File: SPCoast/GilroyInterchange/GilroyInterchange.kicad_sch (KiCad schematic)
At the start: 30 parts, among them SW777 777, SW781 781

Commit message: fix(kicad): approach circuits end in T; desk tokens follow
Plants: Christopher 1NA/2NA/1SA/2SA, GilroyCalTrain 1NA/1SA, GilroyInterchange
1SA, Sargent 1NA/1SA/2SA gain the final T (ADR 0003 D4). Sargent's reference
Corporal:2NA becomes Corporal:2NAT, the circuit Corporal draws.

Desk (South-cTc sheets): IndicationToken follows the plants for Christopher,
GilroyCalTrain, GilroyInterchange; Corporal 1SA becomes 1SAT (the plant already
had it); Christopher 815T2 becomes 815AT1 (the OS circuit of switch 815A).

Not changed, awaiting decisions in the dry-run report: 0<n>T renames (IND,
TK<n>, Interchange, 2NAAT, 2SAT), section 2 of an approach, unnamed circuits,
Watsonville, CP_Watsonville: references, 1TK.

Verified: netlists rebuilt for all affected projects; of 33 desk circuit tokens,
5 now match no plant circuit (was 11): 1TK, CP_Watsonville:SA1,
CP_Watsonville:837T1, Watsonville 1NAK and 2NAK. KiCad closed, no ~*.lck.

Co-Authored-By: Claude Sonnet 5.5 <noreply@anthropic.com>
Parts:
- TC1: value 1SA -> 1SAT
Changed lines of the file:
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@@
 			)
 		)
-		(property "Value" "1SA"
+		(property "Value" "1SAT"
 			(at 61.47 74.68 0)
 			(show_name no)

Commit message: SPCoast: owner's edit: GilroyInterchange 1NAT circuit marker (baseline)
Co-Authored-By: Claude Sonnet 5.5 <noreply@anthropic.com>
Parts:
- added TC4: 1NAT, symbol Railroad:Track Circuit
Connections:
- net at B8.2 (B), CP2.1 (To), DOT1.1: now also TC4.1 (MC)
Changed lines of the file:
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@@
 	)
 	(junction
-		(at 184.15 77.47)
+		(at 196.85 77.47)
 		(diameter 0)
 		(color 0 0 0 0)
@@
 	)
 	(junction
+		(at 182.88 77.47)
+		(diameter 0)
+		(color 0 0 0 0)
+	)
+	(junction
 		(at 120.65 77.47)
 		(diameter 0)
@@
 	(wire
 		(pts
+			(xy 182.88 77.47) (xy 196.85 77.47)
+		)
+		(stroke
+			(width 0.4064)
+			(type default)
+		)
+	)
+	(wire
+		(pts
 			(xy 53.34 77.47) (xy 63.5 77.47)
 		)
@@
 	(wire
 		(pts
-			(xy 170.18 77.47) (xy 184.15 77.47)
+			(xy 170.18 77.47) (xy 182.88 77.47)
 		)
 		(stroke
@@
 	(symbol
 		(lib_id "Railroad:NextCP")
-		(at 184.15 77.47 0)
+		(at 196.85 77.47 0)
 		(unit 1)
 		(body_style 1)
@@
 		(dnp no)
 		(property "Reference" "CP2"
-			(at 187.325 79.375 0)
+			(at 200.025 79.375 0)
 			(hide yes)
 			(show_name no)
@@
 		)
 		(property "Value" "Luchessa"
-			(at 195.834 77.216 0)
+			(at 208.534 77.216 0)
 			(show_name no)
 			(do_not_autoplace no)
@@
 		)
 		(property "Footprint" ""
-			(at 180.34 77.47 0)
+			(at 193.04 77.47 0)
 			(hide yes)
 			(show_name no)
@@
 		)
 		(property "Datasheet" ""
-			(at 180.34 77.47 0)
+			(at 193.04 77.47 0)
 			(hide yes)
 			(show_name no)
@@
 		)
 		(property "Description" "Identifies the next control point on this track"
-			(at 180.975 84.455 0)
+			(at 193.675 84.455 0)
 			(hide yes)
 			(show_name no)
@@
 		)
 		(property "Role" "TRACK"
-			(at 184.15 77.47 0)
+			(at 196.85 77.47 0)
 			(hide yes)
 			(show_name no)
@@
 		)
 		(property "Kind" "NEXT_CP"
-			(at 184.15 77.47 0)
+			(at 196.85 77.47 0)
 			(hide yes)
 			(show_name no)
@@
 		)
 		(property "Direction" ""
-			(at 184.15 77.47 0)
+			(at 196.85 77.47 0)
 			(hide yes)
 			(show_name no)
@@
 		)
 		(property "Name" ""
-			(at 184.15 77.47 0)
+			(at 196.85 77.47 0)
 			(hide yes)
 			(show_name no)
@@
 	)
 	(symbol
+		(lib_id "Railroad:Track Circuit")
+		(at 182.88 77.47 0)
+		(unit 1)
+		(body_style 1)
+		(exclude_from_sim no)
+		(in_bom yes)
+		(on_board yes)
+		(in_pos_files yes)
+		(dnp no)
+		(property "Reference" "TC4"
+			(at 182.88 73.03 0)
+			(hide yes)
+			(show_name no)
+			(do_not_autoplace no)
+			(effects
+				(font
+					(size 1.27 1.27)
+				)
+			)
+		)
+		(property "Value" "1NAT"
+			(at 180.85 74.68 0)
+			(show_name no)
+			(do_not_autoplace no)
+			(effects
+				(font
+					(size 1.27 1.27)
+				)
+				(justify left)
+			)
+		)
+		(property "Footprint" ""
+			(at 182.88 77.47 0)
+			(hide yes)
+			(show_name no)
+			(do_not_autoplace no)
+			(effects
+				(font
+					(size 1.27 1.27)
+				)
+			)
+		)
+		(property "Datasheet" ""
+			(at 182.88 77.47 0)
+			(hide yes)
+			(show_name no)
+			(do_not_autoplace no)
+			(effects
+				(font
+					(size 1.27 1.27)
+				)
+			)
+		)
+		(property "Description" ""
+			(at 182.88 77.47 0)
+			(hide yes)
+			(show_name no)
+			(do_not_autoplace no)
+			(effects
+				(font
+					(size 1.27 1.27)
+				)
+			)
+		)
+		(property "CP" "Gilroy North"
+			(at 182.88 79.37 0)
+			(show_name no)
+			(do_not_autoplace no)
+			(effects
+				(font
+					(size 0.508 0.508)
+					(color 72 72 72 1)
+				)
+			)
+		)
+		(property "Role" "APPLIANCE"
+			(at 182.88 77.47 0)
+			(hide yes)
+			(show_name no)
+			(do_not_autoplace no)
+			(effects
+				(font
+					(size 1.27 1.27)
+				)
+			)
+		)
+		(property "Kind" "TRACK_CIRCUIT"
+			(at 182.88 77.47 0)
+			(hide yes)
+			(show_name no)
+			(do_not_autoplace no)
+			(effects
+				(font
+					(size 1.27 1.27)
+				)
+			)
+		)
+		(property "Direction" ""
+			(at 182.88 77.47 0)
+			(hide yes)
+			(show_name no)
+			(do_not_autoplace no)
+			(effects
+				(font
+					(size 1.27 1.27)
+				)
+			)
+		)
+		(property "Name" ""
+			(at 182.88 77.47 0)
+			(hide yes)
+			(show_name no)
+			(do_not_autoplace no)
+			(effects
+				(font
+					(size 1.27 1.27)
+				)
+			)
+		)
+		(pin "1"
+		)
+		(instances
+			(project "GilroyInterchange"
+				(path "/c4fcbe05-44d0-4e90-8003-c2ec16e00151"
+					(reference "TC4")
+					(unit 1)
+				)
+			)
+		)
+	)
+	(symbol
 		(lib_id "Railroad:NextCP")
 		(at 53.34 77.47 0)
@@
 	(symbol
 		(lib_id "Railroad:Rule261-DoT-BiDirectional")
-		(at 184.15 74.93 0)
+		(at 196.85 74.93 0)
 		(unit 1)
 		(body_style 1)
@@
 		(fields_autoplaced yes)
 		(property "Reference" "DOT1"
-			(at 174.625 73.025 0)
+			(at 187.325 73.025 0)
 			(hide yes)
 			(show_name no)
@@
 		)
 		(property "Value" "Rule 261"
-			(at 184.15 72.39 0)
+			(at 196.85 72.39 0)
 			(show_name no)
 			(do_not_autoplace yes)
@@
 		)
 		(property "Footprint" ""
-			(at 184.15 74.93 0)
+			(at 196.85 74.93 0)
 			(hide yes)
 			(show_name no)
@@
 		)
 		(property "Datasheet" ""
-			(at 184.15 74.93 0)
+			(at 196.85 74.93 0)
 			(hide yes)
 			(show_name no)
@@
 		)
 		(property "Description" "Track Signaled in Both Directions:  Governs bi-directional signal territory (often controlled by  Centralized Traffic Control, or CTC).  Under Rule 261, block signal  indications supersede train superiority for both opposing and following movements on the same track, allowing the dispatcher to dynamically change the direction of traffic by clearing signals."
-			(at 184.15 79.375 0)
+			(at 196.85 79.375 0)
 			(hide yes)
 			(show_name no)
@@
 		)
 		(property "Kind" "RULE_261"
-			(at 184.15 74.93 0)
+			(at 196.85 74.93 0)
 			(hide yes)
 			(show_name no)
@@
 		)
 		(property "Direction" "BOTH"
-			(at 174.625 74.93 0)
+			(at 187.325 74.93 0)
 			(hide yes)
 			(show_name no)
@@
 		)
 		(property "Role" "POLICY"
-			(at 184.15 74.93 0)
+			(at 196.85 74.93 0)
 			(hide yes)
 			(show_name no)
@@
 		)
 		(property "Name" ""
-			(at 184.15 74.93 0)
+			(at 196.85 74.93 0)
 			(hide yes)
 			(show_name no)

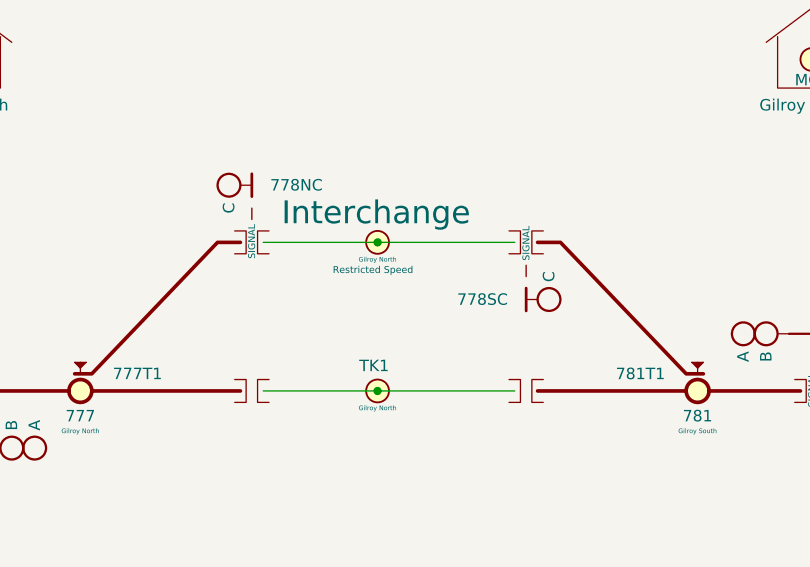
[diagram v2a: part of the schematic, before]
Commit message: fix(kicad): remaining class I circuits take the 0<n>T form
Owner-approved numbers: Luchessa 2SAT -> 02T; Christopher IND -> 01T;
Corporal IND -> 01T; GilroyInterchange Interchange -> 01T and TK1 -> 02T
(passing-track main and siding merged into class I). Desk lamp 1TK on
GilroyInterchange column 4 becomes 02T.

Verified: netlists rebuilt for the five projects; every 0<n>T is unique within
its plant; desk circuit tokens that match no plant circuit are down to four
(CP_Watsonville:SA1, CP_Watsonville:837T1, Watsonville 1NAK and 2NAK).

Co-Authored-By: Claude Sonnet 5.5 <noreply@anthropic.com>
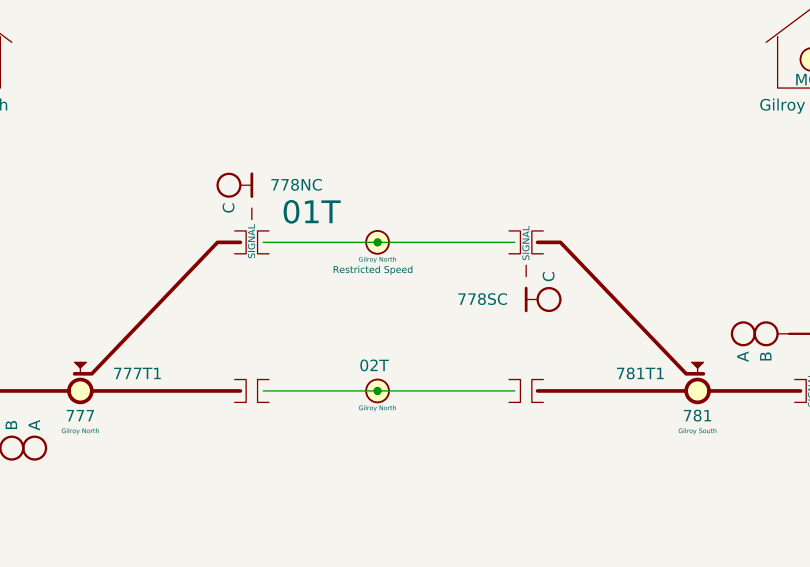
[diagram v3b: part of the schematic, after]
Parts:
- TC2: value TK1 -> 02T
- TC3: value Interchange -> 01T
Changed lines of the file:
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@@
 			)
 		)
-		(property "Value" "Interchange"
+		(property "Value" "01T"
 			(at 109.982 57.658 0)
 			(show_name no)
@@
 			)
 		)
-		(property "Value" "TK1"
+		(property "Value" "02T"
 			(at 118.62 74.68 0)
 			(show_name no)

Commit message: SPCoast: owner's edits: schematics synced with the revised symbol libraries (baseline)
Update Symbols from Library on all plant and desk sheets; CP values for
Christopher, GilroyInterchange and Luchessa; Restricted Speed markers
consolidated in Corporal, Luchessa and Sargent.

Observed in the diff, not changed by the sweep that follows: CP changed on 23
symbols (Christopher: prefix removed, 815/815A/IND now Christopher North) and
added on 12 (GilroyInterchange); two lamps' Color reset to their symbol variant
(Christopher LMP93 red -> yellow, Sargent LMP133 yellow -> red).

Verified: netlists keep their net counts (Christopher 33, Corporal 26,
GilroyCalTrain 27, GilroyInterchange 22, Luchessa 34, Sargent 18, Watsonville
96, South-cTc 341); desk compiles to 75 appliances, 137 bindings, 14 columns;
no root-UUID regression.

Co-Authored-By: Claude Sonnet 5.5 <noreply@anthropic.com>
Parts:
- B1, B3, B7: CP (none) -> Gilroy North
- B2, B4, B8, S2, S4: CP (none) -> Gilroy South
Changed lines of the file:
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@@
 			)
 		)
-		(property "CP" ""
-			(at 76.835 79.375 0)
+		(property "CP" "Gilroy North"
+			(at 74.93 74.93 0)
 			(show_name no)
 			(do_not_autoplace no)
@@
 					(color 72 72 72 1)
 				)
-				(justify right)
 			)
 		)
@@
 			)
 		)
-		(property "CP" ""
-			(at 104.775 59.055 0)
+		(property "CP" "Gilroy North"
+			(at 106.68 63.5 0)
 			(show_name no)
 			(do_not_autoplace no)
@@
 					(color 72 72 72 1)
 				)
-				(justify right)
 			)
 		)
@@
 			)
 		)
-		(property "Description" "Restricted speed: Standard Code Rule 105, GCOR 6.28: This is the foundational rule governing most industrial tracks. It mandates that trains or engines must move at a speed that allows them to stop within half the range of vision short of a train, engine, car, stop signal, derail, or switch improperly lined. It also requires crew members to look out for track obstructions"
+		(property "Description" "Restricted speed: Standard Code Rule 105, GCOR 6.28: Movement on Other Than Main Track. This is the foundational rule governing most industrial tracks. It mandates that trains or engines must move at a speed that allows them to stop within half the range of vision short of a train, engine, car, stop signal, derail, or switch improperly lined. It also requires crew members to look out for track obstructions"
 			(at 123.825 59.055 0)
 			(hide yes)
@@
 			)
 		)
+		(property "CP" "Gilroy North"
+			(at 106.68 77.47 0)
+			(hide yes)
+			(show_name no)
+			(do_not_autoplace no)
+			(effects
+				(font
+					(size 1.27 1.27)
+				)
+			)
+		)
 		(pin "2"
 		)
@@
 			)
 		)
+		(property "CP" "Gilroy South"
+			(at 168.91 73.66 0)
+			(hide yes)
+			(show_name no)
+			(do_not_autoplace no)
+			(effects
+				(font
+					(size 1.27 1.27)
+				)
+			)
+		)
 		(pin "2"
 		)
@@
 			)
 		)
-		(property "Description" "Maintainer Bungalow"
-			(at 168.91 46.36 0)
+		(property "Description" "Rrepresents the Control Point Maintainer Bungalow (plus optional Maintainer Call)"
+			(at 168.91 46.355 0)
 			(hide yes)
 			(show_name no)
@@
 			)
 		)
-		(property "CP" ""
-			(at 167.005 75.565 0)
+		(property "CP" "Gilroy South"
+			(at 168.91 80.01 0)
 			(show_name no)
 			(do_not_autoplace no)
@@
 					(color 72 72 72 1)
 				)
-				(justify right)
 			)
 		)
@@
 			)
 		)
-		(property "CP" ""
-			(at 139.065 62.865 0)
+		(property "CP" "Gilroy South"
+			(at 137.16 58.42 0)
 			(show_name no)
 			(do_not_autoplace no)
@@
 					(color 72 72 72 1)
 				)
-				(justify right)
 			)
 		)
@@
 			)
 		)
+		(property "CP" "Gilroy South"
+			(at 137.16 77.47 0)
+			(hide yes)
+			(show_name no)
+			(do_not_autoplace no)
+			(effects
+				(font
+					(size 1.27 1.27)
+				)
+			)
+		)
 		(pin "1"
 		)
@@
 			)
 		)
-		(property "Description" "Maintainer Bungalow"
-			(at 74.93 46.36 0)
+		(property "Description" "Rrepresents the Control Point Maintainer Bungalow (plus optional Maintainer Call)"
+			(at 74.93 46.355 0)
 			(hide yes)
 			(show_name no)
@@
 			(at 137.16 64.77 0)
 			(hide yes)
+			(show_name no)
+			(do_not_autoplace no)
+			(effects
+				(font
+					(size 1.27 1.27)
+				)
+			)
+		)
+		(property "CP" "Gilroy South"
+			(at 137.16 64.77 0)
+			(hide yes)

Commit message: chore(kicad): sweep instance Role/Kind and stale fields to the library vocabulary
Scripted, one pass over every sheet except Watsonville (open in KiCad, locked):
- Role/Kind of placed symbols refreshed from the library by lib_id: 10 Role
  (MAIN HOUSE CONTROLLED_POINT -> CONTROL_POINT, Rule251-DoT empty) and 17 Kind
  (IRJ-Signal IRJ -> IRJ_SIGNAL x7, Mast_Single/Double swaps, HandThrow
  -> SWITCH_MANUAL, Derail, PanelLock -> LOCK_LEVER, NextCP).
- Stale instance fields dropped where the library no longer has them: 39 Name,
  28 Direction (all empty or retired), 5 CP on Bumper and IRJ symbols.
- Orphan embedded copies of the retired symbol Rule6.28-OtherThanMain removed
  from two sheets (unused).

Not done: Watsonville (locked); CMRInet -> CMRI (library Kind still CMRInet);
fields new to the library (MAIN HOUSE Kind, switch Indications) are not copied
onto instances, the compiler will read library defaults by lib_id; Rulebook
fields stay until the compiler stops requiring them.

Verified: per-symbol before/after comparison shows only these changes, same
symbol sets, positions and lib_ids; netlists keep their net counts (Christopher
33, Corporal 26, GilroyCalTrain 27, GilroyInterchange 22, Luchessa 34, Sargent
18, South-cTc 341); desk still 75 appliances, 137 bindings, 14 columns.

Co-Authored-By: Claude Sonnet 5.5 <noreply@anthropic.com>
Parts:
- B3: CP Gilroy North -> (none)
- B4: CP Gilroy South -> (none)
- DOT3: Name Movement on Other Than Main Track -> (none)
- HOUSE1, HOUSE2: Role CONTROLLED_POINT -> CONTROL_POINT
- S3, S4: Kind MAST_DWARF -> MAST_DOUBLE

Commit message: chore(kicad): masts and maintainer calls carry no CP; IRJ-Signals do; CMRInet Kind is CMRI
Owner decision: an IRJ-Signal is the single source of a signal's control point
(a mast attaches to exactly one IRJ-Signal through its SIGNAL pin); a
maintainer call is tied to its house by the netlist.
- CP dropped from 23 masts and 5 maintainer calls.
- 7 empty IRJ-Signal CPs filled with the plant's only house (Corporal, Sargent).
- 43 empty Name fields that KiCad re-added to Christopher dropped again.
- Codeline-Transport Kind CMRInet -> CMRI on the placed instance and the
  embedded library copy (South-cTc root sheet).

Verified: per-symbol before/after comparison shows only these changes; every
IRJ-Signal in all seven plants has a CP naming one of its plant's houses; net
counts unchanged (Christopher 33, Corporal 26, GilroyCalTrain 27,
GilroyInterchange 22, Luchessa 34, Sargent 18, Watsonville 96, South-cTc 341);
desk compiles to 75 appliances, 137 bindings, 14 columns. Remaining CP
diagnostic: Sargent's Corporal:2NAT placeholder (cross-plant reference).

Co-Authored-By: Claude Sonnet 5.5 <noreply@anthropic.com>
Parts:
- MC1, S1, S3: CP Gilroy North -> (none)
- MC2, S2, S4: CP Gilroy South -> (none)
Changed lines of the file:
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@@
-			)
-		)
-		(property "CP" "Gilroy North"
-			(at 74.93 81.28 0)
-			(hide yes)
-			(show_name no)
-			(do_not_autoplace no)
-			(effects
-				(font
-					(size 1.27 1.27)
-				)
 			)
 		)
@@
 			)
 		)
-		(property "CP" "Gilroy South"
-			(at 168.91 73.66 0)
-			(hide yes)
-			(show_name no)
-			(do_not_autoplace no)
-			(effects
-				(font
-					(size 1.27 1.27)
-				)
-			)
-		)
 		(pin "2"
 		)
@@
 		)
 		(property "Kind" "MAINTAINER_CALL"
-			(at 168.91 40.64 0)
-			(hide yes)
-			(show_name no)
-			(do_not_autoplace no)
-			(effects
-				(font
-					(size 1.27 1.27)
-				)
-			)
-		)
-		(property "CP" "Gilroy South"
 			(at 168.91 40.64 0)
 			(hide yes)
@@
 			)
 		)
-		(property "CP" "Gilroy South"
-			(at 137.16 64.77 0)
-			(hide yes)
-			(show_name no)
-			(do_not_autoplace no)
-			(effects
-				(font
-					(size 1.27 1.27)
-				)
-			)
-		)
 		(pin "2"
 		)
@@
 			)
 		)
-		(property "CP" "Gilroy North"
-			(at 74.93 40.64 0)
-			(hide yes)
-			(show_name no)
-			(do_not_autoplace no)
-			(effects
-				(font
-					(size 1.27 1.27)
-				)
-			)
-		)
 		(pin "1"
 		)
@@
 			(at 106.68 57.15 0)
 			(hide yes)
-			(show_name no)
-			(do_not_autoplace no)
-			(effects
-				(font
-					(size 1.27 1.27)
-				)
-			)
-		)
-		(property "CP" "Gilroy North"
-			(at 106.68 57.15 0)
-			(hide yes)
